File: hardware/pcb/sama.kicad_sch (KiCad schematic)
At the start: 88 parts, among them J4 Conn_ARM_JTAG_SWD_10, J8 Conn_01x02_Pin, U1 SAMA7D65-4HB, Y1 32kHz768, Y2 24MHz

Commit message: mainboard: finished touchpad schematic
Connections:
- net HAPT_~{INT}: no longer names the net of U1.AA19 (PE10)
- no-connect marks 79 -> 80
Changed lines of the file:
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@@
 	)
 	(no_connect
+		(at 135.89 143.51)
+	)
+	(no_connect
 		(at 69.85 148.59)
 	)
@@
 	(wire
 		(pts
-			(xy 135.89 143.51) (xy 138.43 143.51)
-		)
-		(stroke
-			(width 0)
-			(type default)
-		)
-	)
-	(wire
-		(pts
 			(xy 405.13 300.99) (xy 405.13 303.53)
 		)
@@
 		(effects
 			(font
-				(size 1.27 1.27)
-			)
-			(justify left)
-		)
-	)
-	(hierarchical_label "HAPT_~{INT}"
-		(shape input)
-		(at 138.43 143.51 0)
-		(effects
-			(font

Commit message: mainboard: reannotated schematic
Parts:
- removed C89: 4u7, Capacitor_SMD:C_0402_1005Metric, symbol Device:C_Small
- renumbered C27 to C1, C100 to C10, C69 to C11, C84 to C12, C91 to C13, C101 to C14, C70 to C15, C85 to C16, C92 to C17, C102 to C18, C71 to C19, C24 to C2, C86 to C20, C93 to C21, C103 to C22, C72 to C23, C87 to C24, C94 to C25, C104 to C26, C73 to C27, C88 to C28, C95 to C29, C25 to C3, C105 to C30, C74 to C31, C96 to C32, C106 to C33, C75 to C34, C97 to C35, C107 to C36, C76 to C37, C98 to C38, C108 to C39, C99 to C4, C77 to C40, C109 to C41, C78 to C42, C110 to C43, C79 to C44, C111 to C45, C80 to C46, C112 to C47, C81 to C48, C113 to C49, C22 to C5, C82 to C50, C114 to C51, C115 to C52, C119 to C53, C116 to C54, C120 to C55, C117 to C56, C121 to C57, C118 to C58, C122 to C59, C23 to C6, C123 to C60, C124 to C61, C125 to C62, C68 to C7, C83 to C8, C90 to C9, J8 to J1, J4 to J2, JP2 to JP1, JP3 to JP2, R37 to R1, R47 to R10, R48 to R11, R40 to R2, R2 to R3, R36 to R4, R25 to R5, R9 to R6, R10 to R7, R45 to R8, R46 to R9, TP2 to TP1, TP3 to TP2, TP1 to TP3, Y2 to Y1, Y1 to Y2

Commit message: assigned missing footprints
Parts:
- J1: footprint (none) -> Connector_PinHeader_2.54mm:PinHeader_1x02_P2.54mm_Vertical
- JP1, JP2: footprint (none) -> Jumper:SolderJumper-3_P1.3mm_Bridged12_RoundedPad1.0x1.5mm
- TP1, TP2, TP3, TP4, TP5, TP6, TP7: footprint (none) -> TestPoint:TestPoint_Pad_D1.0mm
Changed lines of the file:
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@@
 			)
 		)
-		(property "Footprint" ""
+		(property "Footprint" "TestPoint:TestPoint_Pad_D1.0mm"
 			(at 63.5 100.33 0)
 			(hide yes)
@@
 			)
 		)
-		(property "Footprint" ""
+		(property "Footprint" "TestPoint:TestPoint_Pad_D1.0mm"
 			(at 334.01 231.14 0)
 			(hide yes)
@@
 			)
 		)
-		(property "Footprint" ""
+		(property "Footprint" "TestPoint:TestPoint_Pad_D1.0mm"
 			(at 334.01 226.06 0)
 			(hide yes)
@@
 			)
 		)
-		(property "Footprint" ""
+		(property "Footprint" "Connector_PinHeader_2.54mm:PinHeader_1x02_P2.54mm_Vertical"
 			(at 157.48 95.25 0)
 			(hide yes)
@@
 			)
 		)
-		(property "Footprint" ""
+		(property "Footprint" "TestPoint:TestPoint_Pad_D1.0mm"
 			(at 204.47 227.33 0)
 			(hide yes)
@@
 			)
 		)
-		(property "Footprint" ""
+		(property "Footprint" "TestPoint:TestPoint_Pad_D1.0mm"
 			(at 334.01 228.6 0)
 			(hide yes)
@@
 			)
 		)
-		(property "Footprint" ""
+		(property "Footprint" "TestPoint:TestPoint_Pad_D1.0mm"
 			(at 334.01 233.68 0)
 			(hide yes)
@@
 			)
 		)
-		(property "Footprint" ""
+		(property "Footprint" "TestPoint:TestPoint_Pad_D1.0mm"
 			(at 334.01 241.3 0)
 			(hide yes)
@@
 			)
 		)
-		(property "Footprint" ""
+		(property "Footprint" "Jumper:SolderJumper-3_P1.3mm_Bridged12_RoundedPad1.0x1.5mm"
 			(at 218.44 212.09 0)
 			(hide yes)
@@
 			)
 		)
-		(property "Footprint" ""
+		(property "Footprint" "Jumper:SolderJumper-3_P1.3mm_Bridged12_RoundedPad1.0x1.5mm"
 			(at 387.35 257.81 0)
 			(hide yes)

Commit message: added a bunch testpoints
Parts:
- added TP14: SCL, TestPoint:TestPoint_Pad_D1.0mm, symbol Connector:TestPoint
- added TP17: SDA, TestPoint:TestPoint_Pad_D1.0mm, symbol Connector:TestPoint
- added TP18: T_SCL, TestPoint:TestPoint_Pad_D1.0mm, symbol Connector:TestPoint
- added TP19: T_SDA, TestPoint:TestPoint_Pad_D1.0mm, symbol Connector:TestPoint
- TP2: value ~{TRST} -> PIOBU0
- TP4: value ~{TRST} -> PIOBU1
- TP5: value ~{TRST} -> PIOBU2
- TP6: value ~{TRST} -> PIOBU3
- TP7: value ~{TRST} -> AUDIOCLK
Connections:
- net SCL: now also TP14.1
- net SDA: now also TP17.1
- net TOUCH.SCL: now also TP18.1
- net TOUCH.SDA: now also TP19.1
- net BT.CTSN renamed BT.~{CTS}
- net BT.RTSN renamed BT.~{RTS}
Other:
- moved on the sheet: J1, R1, R2, R4, R5, TP1, U1E

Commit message: removed testpoints on sd cards, since I can probe the pins there
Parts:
- renumbered C2 to C1, C7 to C10, C15 to C12, C19 to C13, C23 to C14, C27 to C15, C31 to C16, C34 to C17, C37 to C18, C40 to C19, C3 to C2, C42 to C20, C44 to C21, C46 to C22, C48 to C23, C50 to C24, C4 to C25, C8 to C26, C12 to C27, C16 to C28, C20 to C29, C5 to C3, C24 to C30, C28 to C31, C53 to C32, C55 to C33, C57 to C34, C59 to C35, C60 to C36, C61 to C37, C62 to C38, C9 to C39, C6 to C4, C13 to C40, C17 to C41, C21 to C42, C25 to C43, C29 to C44, C32 to C45, C35 to C46, C38 to C47, C10 to C48, C14 to C49, C1 to C5, C18 to C50, C22 to C51, C26 to C52, C30 to C53, C33 to C54, C36 to C55, C39 to C56, C41 to C57, C43 to C58, C45 to C59, C52 to C6, C47 to C60, C49 to C61, C51 to C62, C54 to C7, C56 to C8, C58 to C9, R6 to R10, R3 to R11, R4 to R3, R5 to R4, R7 to R5, R8 to R6, R9 to R7, R10 to R8, R11 to R9, TP14 to TP1, TP6 to TP10, TP7 to TP11, TP17 to TP2, TP18 to TP3, TP19 to TP4, TP1 to TP5, TP3 to TP6, TP2 to TP7, TP4 to TP8, TP5 to TP9

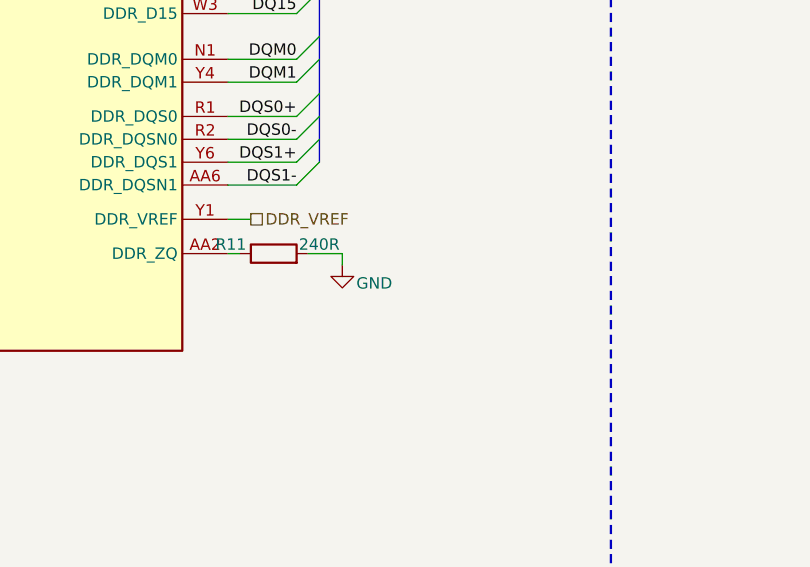
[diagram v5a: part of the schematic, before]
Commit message: added capacitor to sama ddr vref pin
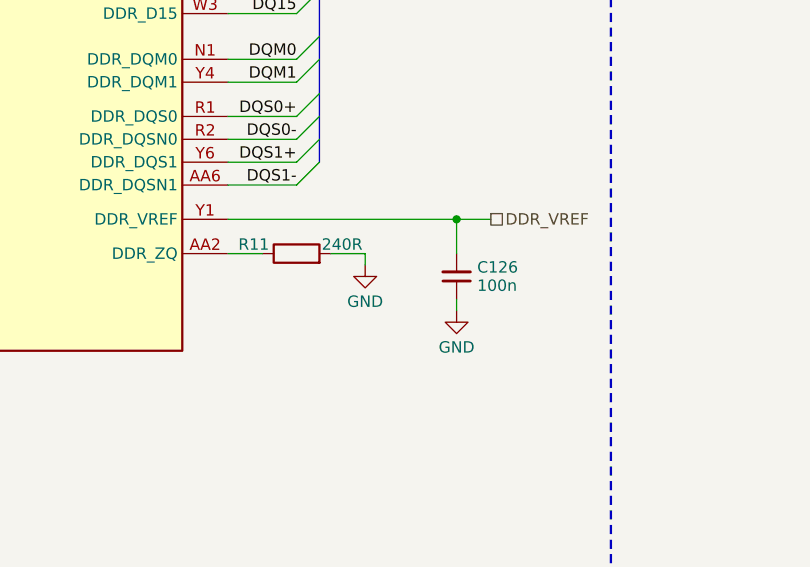
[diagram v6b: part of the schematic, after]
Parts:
- added C126: 100n, Capacitor_SMD:C_0402_1005Metric, symbol Device:C_Small
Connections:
- net DDR_VREF: now also C126.2
- net GND: now also C126.1
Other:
- moved on the sheet: R11

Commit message: didn't save last time :sob:
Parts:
- renumbered C9 to C10, C10 to C11, C11 to C12, C12 to C13, C13 to C14, C14 to C15, C15 to C16, C16 to C17, C17 to C18, C18 to C19, C19 to C20, C20 to C21, C21 to C22, C22 to C23, C23 to C24, C24 to C25, C25 to C26, C26 to C27, C27 to C28, C28 to C29, C29 to C30, C30 to C31, C31 to C32, C32 to C33, C33 to C34, C34 to C35, C35 to C36, C36 to C37, C37 to C38, C38 to C39, C39 to C40, C40 to C41, C41 to C42, C42 to C43, C43 to C44, C44 to C45, C45 to C46, C46 to C47, C47 to C48, C48 to C49, C49 to C50, C50 to C51, C51 to C52, C52 to C53, C53 to C54, C54 to C55, C55 to C56, C56 to C57, C57 to C58, C58 to C59, C126 to C6, C59 to C60, C60 to C61, C61 to C62, C62 to C63, C6 to C7, C7 to C8, C8 to C9

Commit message: grouped pwr pins, made small improvements
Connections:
- net +1V15_CORE: now also U1.[B2,F6,F15,H3,J9,J13,J16,N13,N16,T15,U16,U17,U19,V19] (VDDCORE); no longer U1.B2 (VDDCORE), U1.F15 (VDDCORE), U1.F6 (VDDCORE), U1.H3 (VDDCORE), U1.J13 (VDDCORE), U1.J16 (VDDCORE), U1.J9 (VDDCORE), U1.N13 (VDDCORE), U1.N16 (VDDCORE), U1.T15 (VDDCORE), U1.U16 (VDDCORE), U1.U17 (VDDCORE), U1.U19 (VDDCORE), U1.V19 (VDDCORE)
- net +1V15_CPU: now also U1.[B20,E16,E17,E19,F17] (VDDCPU); no longer U1.B20 (VDDCPU), U1.E16 (VDDCPU), U1.E17 (VDDCPU), U1.E19 (VDDCPU), U1.F17 (VDDCPU)
- net +1V35_DDR: now also U1.[AA5,M11,N6,N9,N12,P3,P13,T6,T7,T9,U3,U5,U6,W8,Y2] (VDDIODDR); no longer U1.AA5 (VDDIODDR), U1.M11 (VDDIODDR), U1.N12 (VDDIODDR), U1.N6 (VDDIODDR), U1.N9 (VDDIODDR), U1.P13 (VDDIODDR), U1.P3 (VDDIODDR), U1.T6 (VDDIODDR), U1.T7 (VDDIODDR), U1.T9 (VDDIODDR), U1.U3 (VDDIODDR), U1.U5 (VDDIODDR), U1.U6 (VDDIODDR), U1.W8 (VDDIODDR), U1.Y2 (VDDIODDR)
- net +2V5: now also U1.[E5,J6] (VDDANA); no longer U1.E5 (VDDANA), U1.J6 (VDDANA)
- net GND: now also U1.[A1,A11,A14,A17,A21,AA1,AA8,AA9,AA11,AA14,AA17,AA21,B6,C4,C7,D9,D13,E15,E21,F16,G15,G17,H8,H9,H14,H21,J4,J18,K11,L1,L11,L15,L21,N4,N18,P1,P8,P14,P21,R5,R7,R11,R17,T5,T17,U1,U7,U21,V13,W5] (GND), U1.[E1,E7,H1,V9] (GNDANA), U1.[R15,U15] (GNDDPHY); no longer U1.A1 (GND), U1.A11 (GND), U1.A14 (GND), U1.A17 (GND), U1.A21 (GND), U1.AA1 (GND), U1.AA11 (GND), U1.AA14 (GND), U1.AA17 (GND), U1.AA21 (GND), U1.AA8 (GND), U1.AA9 (GND), U1.B6 (GND), U1.C4 (GND), U1.C7 (GND), U1.D13 (GND), U1.D9 (GND), U1.E1 (GNDANA), U1.E15 (GND), U1.E21 (GND), U1.E7 (GNDANA), U1.F16 (GND), U1.G15 (GND), U1.G17 (GND), U1.H1 (GNDANA), U1.H14 (GND), U1.H21 (GND), U1.H8 (GND), U1.H9 (GND), U1.J18 (GND), U1.J4 (GND), U1.K11 (GND), U1.L1 (GND), U1.L11 (GND), U1.L15 (GND), U1.L21 (GND), U1.N18 (GND), U1.N4 (GND), U1.P1 (GND), U1.P14 (GND), U1.P21 (GND), U1.P8 (GND), U1.R11 (GND), U1.R15 (GNDDPHY), U1.R17 (GND), U1.R5 (GND), U1.R7 (GND), U1.T17 (GND), U1.T5 (GND), U1.U1 (GND), U1.U15 (GNDDPHY), U1.U21 (GND), U1.U7 (GND), U1.V13 (GND), U1.V9 (GNDANA), U1.W5 (GND)
- no-connect marks 80 -> 87
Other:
- moved on the sheet: JP2, U1A
